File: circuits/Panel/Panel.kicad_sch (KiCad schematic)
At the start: 0 parts

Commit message: panelフットプリント配置
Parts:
- added H1, H11, H12, H13, H14, H2, H3, H4, H6, H7, H8, H9: MountingHole_Pad, TestPoint:TestPoint_Pad_2.0x2.0mm, symbol Mechanical:MountingHole_Pad
- added H10, H5: MountingHole_Pad, TestPoint:TestPoint_Pad_3.0x3.0mm, symbol Mechanical:MountingHole_Pad
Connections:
- new net DIN0: H1.1
- new net DIN1: H3.1
- new net DIN2: H6.1
- new net DIN3: H8.1
- new net DIN4: H11.1
- new net DIN5: H13.1
- new net DOUT0: H2.1
- new net DOUT1: H4.1
- new net DOUT2: H7.1
- new net DOUT3: H9.1
- new net DOUT4: H12.1
- new net DOUT5: H14.1
- new net GND: H10.1
- new net VDD: H5.1
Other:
- added sheet NeoPixel (NeoPixel.kicad_sch)
- added sheet Pass_con (Pass_con.kicad_sch)
- note added: "Conn Pad"
- note added: "Power Pad"
- note added: "Signal IN Pad"
- note added: "Signal OUT Pad"

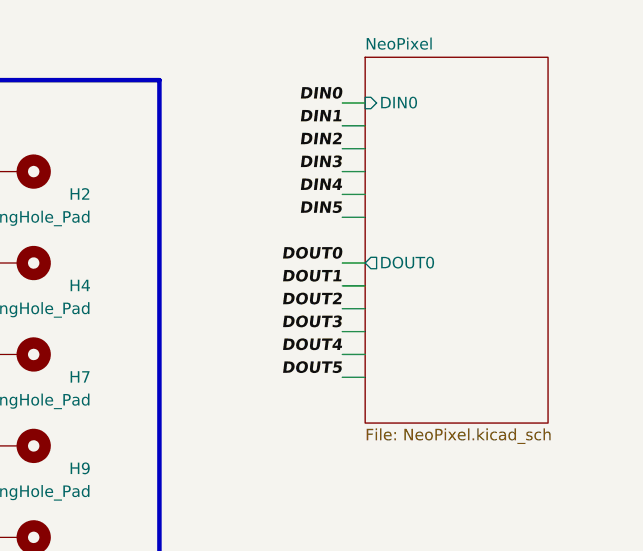
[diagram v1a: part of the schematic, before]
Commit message: シンボル・フットプリントMyLib->TomoshibiLib置き換え
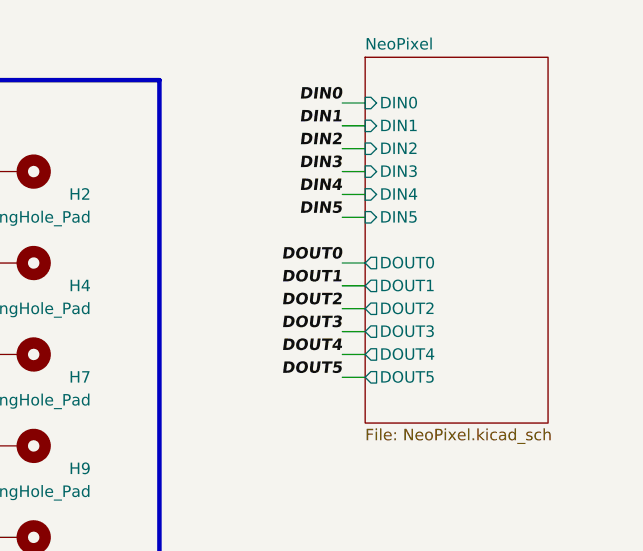
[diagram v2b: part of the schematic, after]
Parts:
- H1, H11, H12, H13, H14, H2, H3, H4, H6, H7, H8, H9: footprint TestPoint:TestPoint_Pad_2.0x2.0mm -> TestPoint:TestPoint_Pad_D2.0mm
- H10, H5: footprint TestPoint:TestPoint_Pad_3.0x3.0mm -> TestPoint:TestPoint_Pad_D3.0mm
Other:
- sheet NeoPixel ports: added DIN1, DIN2, DIN3, DIN4, DIN5, DOUT1, DOUT2, DOUT3, DOUT4, DOUT5; removed none
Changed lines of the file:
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@@
       (effects (font (size 1.27 1.27)) (justify right))
     )
-    (property "Footprint" "TestPoint:TestPoint_Pad_2.0x2.0mm" (at 124.46 78.74 0)
+    (property "Footprint" "TestPoint:TestPoint_Pad_D2.0mm" (at 124.46 78.74 0)
       (effects (font (size 1.27 1.27)) hide)
     )
@@
       (effects (font (size 1.27 1.27)) (justify right))
     )
-    (property "Footprint" "TestPoint:TestPoint_Pad_2.0x2.0mm" (at 124.46 88.9 0)
+    (property "Footprint" "TestPoint:TestPoint_Pad_D2.0mm" (at 124.46 88.9 0)
       (effects (font (size 1.27 1.27)) hide)
     )
@@
       (effects (font (size 1.27 1.27)) (justify right))
     )
-    (property "Footprint" "TestPoint:TestPoint_Pad_2.0x2.0mm" (at 124.46 129.54 0)
+    (property "Footprint" "TestPoint:TestPoint_Pad_D2.0mm" (at 124.46 129.54 0)
       (effects (font (size 1.27 1.27)) hide)
     )
@@
       (effects (font (size 1.27 1.27)) (justify right))
     )
-    (property "Footprint" "TestPoint:TestPoint_Pad_2.0x2.0mm" (at 160.02 129.54 0)
+    (property "Footprint" "TestPoint:TestPoint_Pad_D2.0mm" (at 160.02 129.54 0)
       (effects (font (size 1.27 1.27)) hide)
     )
@@
       (effects (font (size 1.27 1.27)) (justify right))
     )
-    (property "Footprint" "TestPoint:TestPoint_Pad_2.0x2.0mm" (at 160.02 109.22 0)
+    (property "Footprint" "TestPoint:TestPoint_Pad_D2.0mm" (at 160.02 109.22 0)
       (effects (font (size 1.27 1.27)) hide)
     )
@@
       (effects (font (size 1.27 1.27)) (justify right))
     )
-    (property "Footprint" "TestPoint:TestPoint_Pad_2.0x2.0mm" (at 160.02 99.06 0)
+    (property "Footprint" "TestPoint:TestPoint_Pad_D2.0mm" (at 160.02 99.06 0)
       (effects (font (size 1.27 1.27)) hide)
     )
@@
       (effects (font (size 1.27 1.27)) (justify right))
     )
-    (property "Footprint" "TestPoint:TestPoint_Pad_3.0x3.0mm" (at 96.52 111.76 0)
+    (property "Footprint" "TestPoint:TestPoint_Pad_D3.0mm" (at 96.52 111.76 0)
       (effects (font (size 1.27 1.27)) hide)
     )
@@
       (effects (font (size 1.27 1.27)) (justify right))
     )
-    (property "Footprint" "TestPoint:TestPoint_Pad_2.0x2.0mm" (at 124.46 99.06 0)
+    (property "Footprint" "TestPoint:TestPoint_Pad_D2.0mm" (at 124.46 99.06 0)
       (effects (font (size 1.27 1.27)) hide)
     )
@@
       (effects (font (size 1.27 1.27)) (justify right))
     )
-    (property "Footprint" "TestPoint:TestPoint_Pad_2.0x2.0mm" (at 160.02 78.74 0)
+    (property "Footprint" "TestPoint:TestPoint_Pad_D2.0mm" (at 160.02 78.74 0)
       (effects (font (size 1.27 1.27)) hide)
     )
@@
       (effects (font (size 1.27 1.27)) (justify right))
     )
-    (property "Footprint" "TestPoint:TestPoint_Pad_2.0x2.0mm" (at 124.46 109.22 0)
+    (property "Footprint" "TestPoint:TestPoint_Pad_D2.0mm" (at 124.46 109.22 0)
       (effects (font (size 1.27 1.27)) hide)
     )
@@
       (effects (font (size 1.27 1.27)) (justify right))
     )
-    (property "Footprint" "TestPoint:TestPoint_Pad_2.0x2.0mm" (at 160.02 119.38 0)
+    (property "Footprint" "TestPoint:TestPoint_Pad_D2.0mm" (at 160.02 119.38 0)
       (effects (font (size 1.27 1.27)) hide)
     )
@@
       (effects (font (size 1.27 1.27)) (justify right))
     )
-    (property "Footprint" "TestPoint:TestPoint_Pad_2.0x2.0mm" (at 160.02 88.9 0)
+    (property "Footprint" "TestPoint:TestPoint_Pad_D2.0mm" (at 160.02 88.9 0)
       (effects (font (size 1.27 1.27)) hide)
     )
@@
       (effects (font (size 1.27 1.27)) (justify right))
     )
-    (property "Footprint" "TestPoint:TestPoint_Pad_3.0x3.0mm" (at 96.52 96.52 0)
+    (property "Footprint" "TestPoint:TestPoint_Pad_D3.0mm" (at 96.52 96.52 0)
       (effects (font (size 1.27 1.27)) hide)
     )
@@
       (effects (font (size 1.27 1.27)) (justify right))
     )
-    (property "Footprint" "TestPoint:TestPoint_Pad_2.0x2.0mm" (at 124.46 119.38 0)
+    (property "Footprint" "TestPoint:TestPoint_Pad_D2.0mm" (at 124.46 119.38 0)
       (effects (font (size 1.27 1.27)) hide)
     )
@@
       (effects (font (size 1.27 1.27)) (justify left))
     )
+    (pin "DIN2" input (at 198.12 76.2 180)
+      (effects (font (size 1.27 1.27)) (justify left))
+    )
+    (pin "DIN1" input (at 198.12 73.66 180)
+      (effects (font (size 1.27 1.27)) (justify left))
+    )
+    (pin "DIN3" input (at 198.12 78.74 180)
+      (effects (font (size 1.27 1.27)) (justify left))
+    )
+    (pin "DIN4" input (at 198.12 81.28 180)
+      (effects (font (size 1.27 1.27)) (justify left))
+    )
+    (pin "DIN5" input (at 198.12 83.82 180)
+      (effects (font (size 1.27 1.27)) (justify left))
+    )
+    (pin "DOUT4" output (at 198.12 99.06 180)
+      (effects (font (size 1.27 1.27)) (justify left))
+    )
+    (pin "DOUT3" output (at 198.12 96.52 180)
+      (effects (font (size 1.27 1.27)) (justify left))
+    )
+    (pin "DOUT5" output (at 198.12 101.6 180)
+      (effects (font (size 1.27 1.27)) (justify left))
+    )
+    (pin "DOUT2" output (at 198.12 93.98 180)
+      (effects (font (size 1.27 1.27)) (justify left))
+    )
+    (pin "DOUT1" output (at 198.12 91.44 180)
+      (effects (font (size 1.27 1.27)) (justify left))
+    )

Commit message: 配線おけ
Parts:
- added H15, H16, H17, H18, H19, H20, H21, H22, H23, H24, H25, H26, H27, H28: MountingHole_Pad, TestPoint:TestPoint_Pad_4.0x4.0mm, symbol Mechanical:MountingHole_Pad
- H10, H5: footprint TestPoint:TestPoint_Pad_D3.0mm -> TestPoint:TestPoint_Pad_4.0x4.0mm
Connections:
- net GND: now also H16.1, H18.1, H20.1, H25.1, H26.1, H27.1, H28.1
- net VDD: now also H15.1, H17.1, H19.1, H21.1, H22.1, H23.1, H24.1
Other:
- moved on the sheet: H10, H5

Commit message: 更新
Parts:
- added H29, H30, H31, H32: MountingHole, TomoshibiLibrary:Pad_MountingPad_D8.0mm, symbol Mechanical:MountingHole
- H10, H15, H16, H17, H18, H19, H20, H21, H22, H23, H24, H25, H26, H27, H28, H5: footprint TestPoint:TestPoint_Pad_4.0x4.0mm -> TestPoint:TestPoint_Pad_D4.0mm
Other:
- note added: "固定用パッド"
